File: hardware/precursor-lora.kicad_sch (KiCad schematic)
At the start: 12 parts, among them J1 PRECURSOR, J2 U.FL, U1 RAK3172, U2 AP2112K-3.3

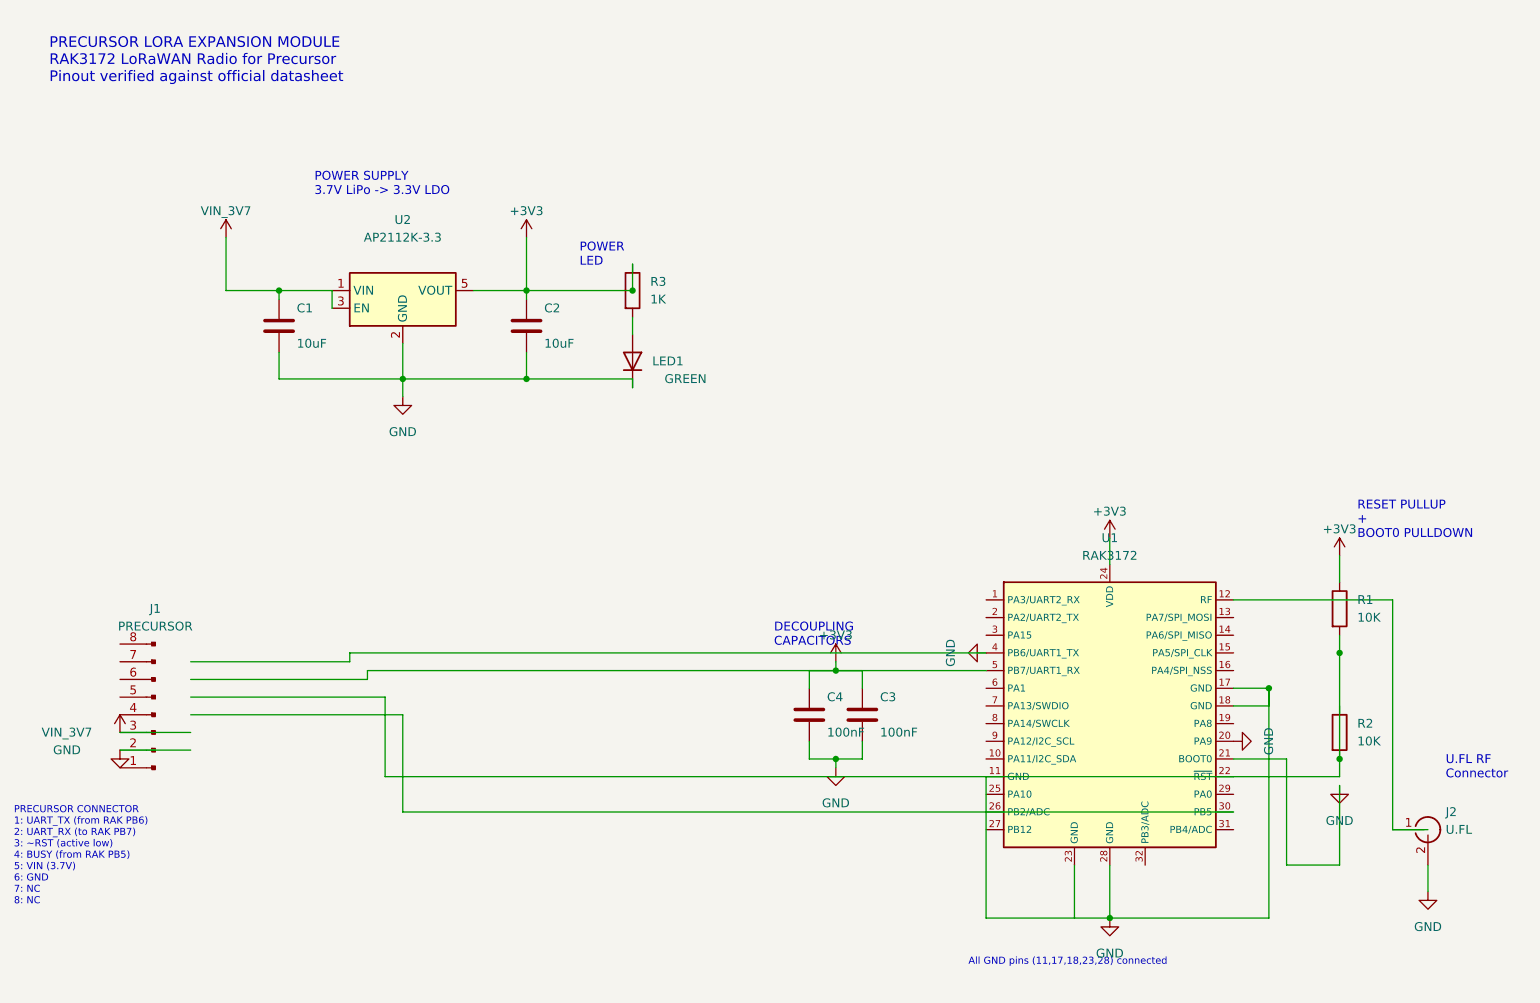
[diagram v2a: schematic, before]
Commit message: WIP: PCB routing in progress - board outline, zones, partial traces
Schematic:
- All components properly connected
- ERC passes with 0 errors (31 warnings for lib symbol mismatches)
- Net assignments verified for all signals

PCB Layout:
- Board outline: 50x30mm on Edge.Cuts layer
- GND zone on F.Cu and B.Cu with proper fills
- All footprints imported via "Update PCB from Schematic"
- J2 (U.FL) keepout zone properly defined

Routing (in progress):
- Added route_pcb.py script for programmatic trace generation
- 45 segments, 10 vias placed
- Remaining DRC issues to resolve:
  - Some trace crossings on B.Cu
  - Clearance violations near J1 connector area
  - Thermal relief issues on GND pads

Next steps:
- Complete routing with proper clearances
- Resolve all DRC errors
- Generate Gerber files for manufacturing

Co-Authored-By: Claude Opus 4.5 <noreply@anthropic.com>
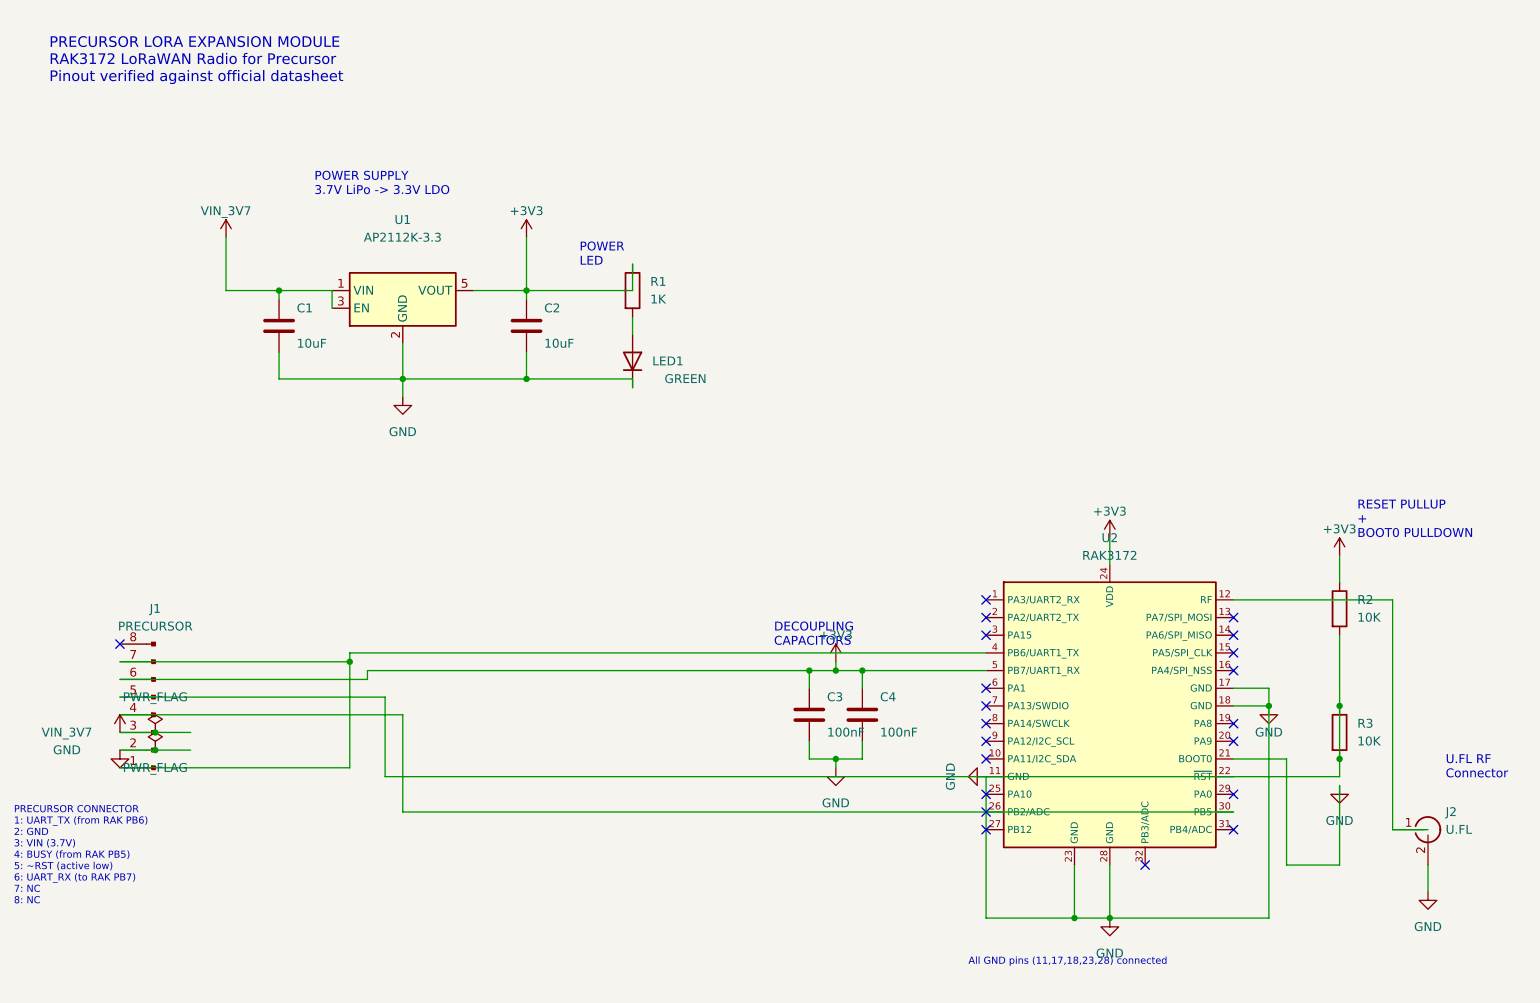
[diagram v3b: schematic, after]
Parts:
- removed U1: RAK3172, PrecursorLoRa:RAK3172, symbol PrecursorLoRa:RAK3172
- removed U2: AP2112K-3.3, Package_TO_SOT_SMD:SOT-23-5, symbol Regulator_Linear:AP2112K-3.3
- added U1: AP2112K-3.3, Package_TO_SOT_SMD:SOT-23-5, symbol Regulator_Linear:AP2112K-3.3
- added U2: RAK3172, PrecursorLoRa:RAK3172, symbol PrecursorLoRa:RAK3172
- R1: value 10K -> 1K; MPN RC0402FR-0710KL -> RC0402FR-071KL
- R3: value 1K -> 10K; MPN RC0402FR-071KL -> RC0402FR-0710KL
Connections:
- net +3V3: now also J1.6 (Pin_6), R2.1, U1.5 (VOUT), U2.24 (VDD), U2.5 (PB7/UART1_RX); no longer R3.1
- net GND: now also U1.2 (GND), U2.11 (GND), U2.17 (GND), U2.18 (GND), U2.21 (BOOT0), U2.23 (GND), U2.28 (GND)
- net VIN_3V7: now also U1.1 (VIN), U1.3 (EN)
- net at J1.1 (Pin_1): now also J1.7 (Pin_7), U2.4 (PB6/UART1_TX)
- net at J1.4 (Pin_4): now also U2.30 (PB5)
- net at J1.5 (Pin_5): now also R2.2, R3.1, R3.2, U2.22 (~{RST})
- net at J2.1 (In): now also U2.12 (RF)
- net at LED1.2 (A): now also R1.2; no longer R3.2
- no-connect marks 0 -> 21
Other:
- note added: "PRECURSOR CONNECTOR 1: UART_TX (from RAK PB6) 2: GND 3: VIN (3.7V) 4: BUSY (from RAK PB5) 5: ~RST (active low) 6: UART_RX (to RAK PB7) 7: NC 8: NC"
- note removed: "PRECURSOR CONNECTOR 1: UART_TX (from RAK PB6) 2: UART_RX (to RAK PB7) 3: ~RST (active low) 4: BUSY (from RAK PB5) 5: VIN (3.7V) 6: GND 7: NC 8: NC"
